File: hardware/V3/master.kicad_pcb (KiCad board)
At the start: 4 copper layers, 40 x 40 mm, 141 parts, among them J1 USB-C, J2 DRILL, J3 DRILL, J4 DRILL, J5 DRILL, J6 STACK-UP-LOW, J7 STACK-DOWN, J8 STACK-UP-LOW, J9 STACK-DOWN, P1 Port A, P2 Port B, P3 Port C, P4 Port D, P5 TSTPT_GND, P6 TSTPT_5V, P7 TSTPT_3V3, P8 Bricklet 5V, P9 Bricklet 3,3V, Q1 2N7002P, SW1 Reset, SW2 Erase, U1 SAM???, U12 LD1117, U13 STMPS2171STR, U2 82400152, U3 TPS22975, U4 AP7333-33SRG, U5 AP7333-33SRG, X1 16Mhz

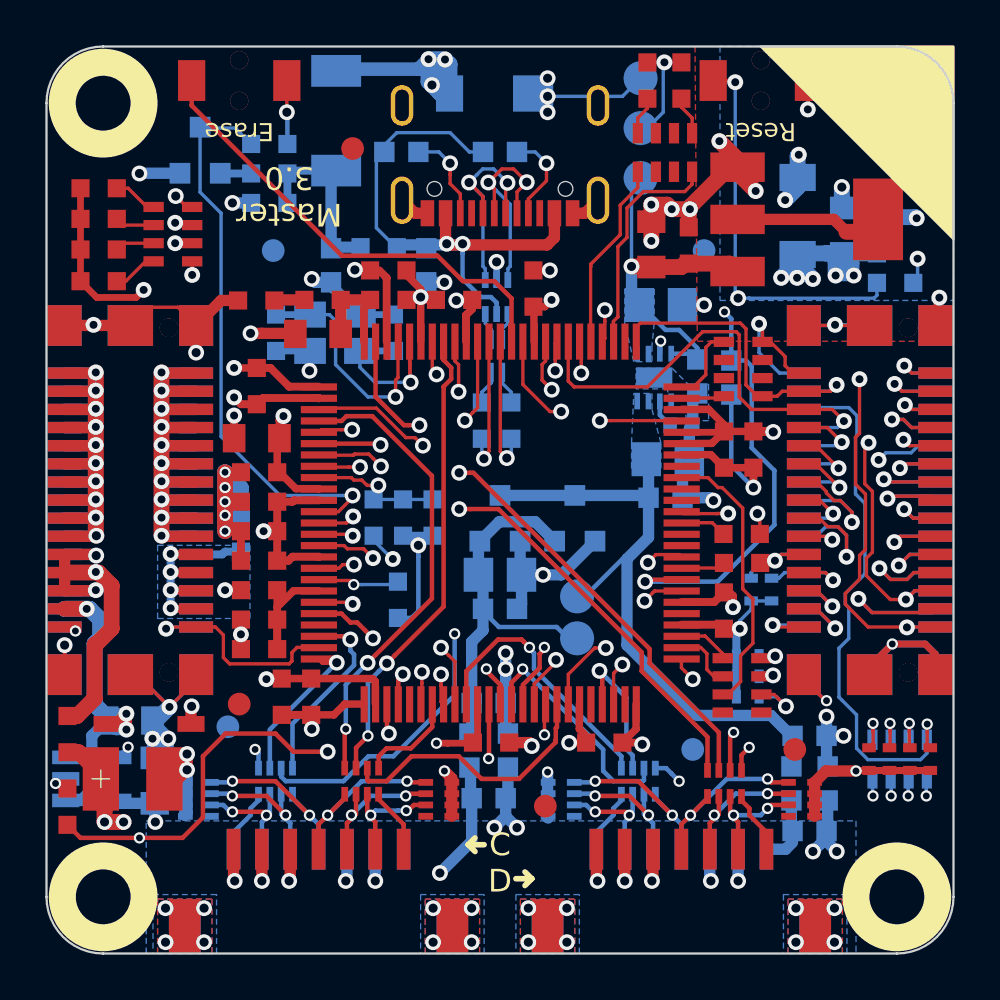
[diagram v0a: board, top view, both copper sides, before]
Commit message: add series resistors for stack connections, change signal connections
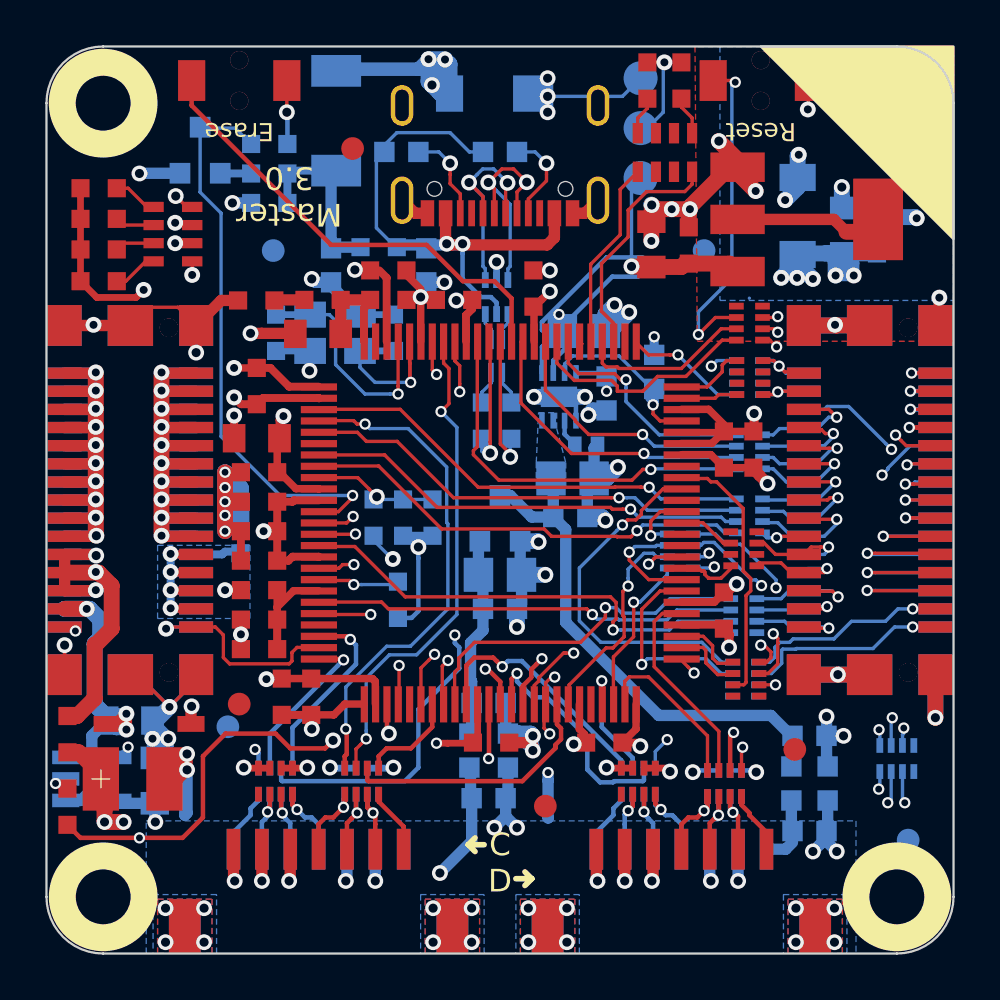
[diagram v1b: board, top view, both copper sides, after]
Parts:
- removed C1, C2, C3, C4, C5, C6, C7, C8, C9: DNP, C0402
- removed P8: Bricklet 5V, kicad-libraries:TSTPT
- removed P9: Bricklet 3,3V, kicad-libraries:TSTPT
- removed R1, R2: 100, R0603
- removed R14: 1k, R0603
- removed RP1, RP2: 100, 0603X4
- removed U5: AP7333-33SRG, kicad-libraries:SOT23-3
- added RP301: 82, kicad-libraries:4X0402, B.Cu at (156.0, 87.9)
- added RP302: 82, kicad-libraries:4X0402, B.Cu at (156.0, 90.7)
- added RP303: 82, kicad-libraries:4X0402, F.Cu at (155.8, 92.2)
- added RP304: 82, kicad-libraries:4X0402, B.Cu at (155.8, 95.1)
- added RP305: 82, kicad-libraries:4X0402, B.Cu at (162.5, 101.4)
- added RP306: 82, kicad-libraries:4X0402, F.Cu at (155.8, 97.9)
- added RP307: 82, kicad-libraries:4X0402, B.Cu at (152.9, 92.2)
- added RP308: 82, kicad-libraries:4X0402, B.Cu at (155.8, 97.9)
- added RP309: 1k, kicad-libraries:4X0402, F.Cu at (156.0, 82.2)
- added RP310: 82, kicad-libraries:4X0402, B.Cu at (156.0, 84.6)
- CP1, CP2: moved to F.Cu
- CP3, CP4: moved to B.Cu
- RP8: footprint 0603X4 -> kicad-libraries:4X0402
- moved Fiducial_Mark 10.3 mm to (163.0, 105.0)
- moved U3 4.29 mm to (147.6, 85.5)
- moved C41 4.29 mm to (148.2, 89.0)
- moved C42 4.29 mm to (148.1, 90.8)
- moved C40 4.29 mm to (148.8, 87.5)
- moved C14 4.07 mm to (149.7, 85.3)
- moved C45 3.59 mm to (148.7, 82.5)
- moved CP1 3.49 mm to (135.1, 102.4), turned to 0 degrees
- moved CP2 3.49 mm to (151.1, 102.4), turned to 0 degrees
- moved CP3 3.49 mm to (138.9, 102.4), turned to 180 degrees
- moved CP4 3.47 mm to (154.9, 102.5), turned to 180 degrees
- moved R7 3.41 mm to (151.8, 84.3), turned to 270 degrees
- moved RP8 0.48 mm to (156.0, 84.6), turned to 90 degrees
- moved FB3 0.08 mm to (133.6, 91.5), turned to 90 degrees
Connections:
- FB3 pad 1: GND -> Net-(FB3-Pad1)
- FB3 pad 2: Net-(FB3-Pad2) -> GND
- J6 pad 1: STACK-SPI-MISO -> Net-(J6-Pad1)
- J6 pad 10: STACK-SELECT-02 -> Net-(J6-Pad10)
- J6 pad 11: STACK-SYNC/JTAG-TCK -> Net-(J6-Pad11)
- J6 pad 12: STACK-SELECT-03 -> Net-(J6-Pad12)
- J6 pad 13: STACK-SER-RXD -> Net-(J6-Pad13)
- J6 pad 14: STACK-SELECT-04 -> Net-(J6-Pad14)
- J6 pad 15: STACK-SER-TXD -> Net-(J6-Pad15)
- J6 pad 16: STACK-SELECT-05 -> Net-(J6-Pad16)
- J6 pad 17: STACK-SER-SCK -> Net-(J6-Pad17)
- J6 pad 18: STACK-SELECT-06 -> Net-(J6-Pad18)
- J6 pad 19: STACK-EX-0-GP00 -> Net-(J6-Pad19)
- J6 pad 2: STACK-I2C-SDA/JTAG-TDI -> Net-(J6-Pad2)
- J6 pad 20: STACK-SELECT-07 -> Net-(J6-Pad20)
- J6 pad 21: STACK-EX-0-GP01 -> Net-(J6-Pad21)
- J6 pad 22: STACK-SELECT-EX-00 -> Net-(J6-Pad22)
- J6 pad 23: STACK-EX-0-GP02 -> Net-(J6-Pad23)
- J6 pad 24: STACK-SELECT-EX-01 -> Net-(J6-Pad24)
- J6 pad 25: STACK-EX-1-GP00 -> Net-(J6-Pad25)
- J6 pad 26: STACK-SER2-RXD -> Net-(J6-Pad26)
- J6 pad 27: STACK-EX-1-GP01 -> Net-(J6-Pad27)
- J6 pad 28: STACK-SER2-TXD -> Net-(J6-Pad28)
- J6 pad 29: STACK-EX-1-GP02 -> Net-(J6-Pad29)
- J6 pad 3: STACK-SPI-MOSI -> Net-(J6-Pad3)
- J6 pad 30: STACK-SER2-RTS -> Net-(J6-Pad30)
- J6 pad 4: STACK-I2C-SCL/JTAG-TDO -> Net-(J6-Pad4)
- J6 pad 5: STACK-SPI-SCLK -> Net-(J6-Pad5)
- J6 pad 6: STACK-SELECT-00 -> Net-(J6-Pad6)
- J6 pad 8: STACK-SELECT-01 -> Net-(J6-Pad8)
- J6 pad 9: STACK-HIGH/JTAG-TMS -> Net-(J6-Pad9)
- J7 pad 1: STACK-SPI-MISO -> Net-(J6-Pad1)
- J7 pad 10: STACK-SELECT-01 -> Net-(J6-Pad8)
- J7 pad 11: STACK-SYNC/JTAG-TCK -> Net-(J6-Pad11)
- J7 pad 12: STACK-SELECT-02 -> Net-(J6-Pad10)
- J7 pad 13: STACK-SER-RXD -> Net-(J6-Pad13)
- J7 pad 14: STACK-SELECT-03 -> Net-(J6-Pad12)
- J7 pad 15: STACK-SER-TXD -> Net-(J6-Pad15)
- J7 pad 16: STACK-SELECT-04 -> Net-(J6-Pad14)
- J7 pad 17: STACK-SER-SCK -> Net-(J6-Pad17)
- J7 pad 18: STACK-SELECT-05 -> Net-(J6-Pad16)
- J7 pad 19: STACK-EX-0-GP00 -> Net-(J6-Pad19)
- J7 pad 2: STACK-I2C-SDA/JTAG-TDI -> Net-(J6-Pad2)
- J7 pad 20: STACK-SELECT-06 -> Net-(J6-Pad18)
- J7 pad 21: STACK-EX-0-GP01 -> Net-(J6-Pad21)
- J7 pad 22: STACK-SELECT-EX-00 -> Net-(J6-Pad22)
- J7 pad 23: STACK-EX-0-GP02 -> Net-(J6-Pad23)
- J7 pad 24: STACK-SELECT-EX-01 -> Net-(J6-Pad24)
- J7 pad 25: STACK-EX-1-GP00 -> Net-(J6-Pad25)
- J7 pad 26: STACK-SER2-RXD -> Net-(J6-Pad26)
- J7 pad 27: STACK-EX-1-GP01 -> Net-(J6-Pad27)
- J7 pad 28: STACK-SER2-TXD -> Net-(J6-Pad28)
- J7 pad 29: STACK-EX-1-GP02 -> Net-(J6-Pad29)
- J7 pad 3: STACK-SPI-MOSI -> Net-(J6-Pad3)
- J7 pad 30: STACK-SER2-RTS -> Net-(J6-Pad30)
- J7 pad 4: STACK-I2C-SCL/JTAG-TDO -> Net-(J6-Pad4)
- J7 pad 5: STACK-SPI-SCLK -> Net-(J6-Pad5)
- J7 pad 8: STACK-SELECT-00 -> Net-(J6-Pad6)
- J8 pad 21: Net-(FB3-Pad2) -> Net-(FB3-Pad1)
- J8 pad 23: Net-(FB3-Pad2) -> Net-(FB3-Pad1)
- J8 pad 25: Net-(FB3-Pad2) -> Net-(FB3-Pad1)
- J8 pad 27: Net-(FB3-Pad2) -> Net-(FB3-Pad1)
- J9 pad 21: Net-(FB3-Pad2) -> Net-(FB3-Pad1)
- J9 pad 23: Net-(FB3-Pad2) -> Net-(FB3-Pad1)
- J9 pad 25: Net-(FB3-Pad2) -> Net-(FB3-Pad1)
- J9 pad 27: Net-(FB3-Pad2) -> Net-(FB3-Pad1)
- P1 pad 4: Net-(CP1-Pad1) -> Net-(CP1-Pad4)
- P1 pad 5: Net-(CP1-Pad2) -> Net-(CP1-Pad3)
- P1 pad 6: Net-(CP1-Pad3) -> Net-(CP1-Pad2)
- P2 pad 4: Net-(CP2-Pad1) -> Net-(CP2-Pad4)
- P2 pad 5: Net-(CP2-Pad2) -> Net-(CP2-Pad3)
- P2 pad 6: Net-(CP2-Pad3) -> Net-(CP2-Pad2)
- P3 pad 4: Net-(CP3-Pad1) -> Net-(CP3-Pad4)
- P3 pad 5: Net-(CP3-Pad2) -> Net-(CP3-Pad3)
- P3 pad 6: Net-(CP3-Pad3) -> Net-(CP3-Pad2)
- P4 pad 4: Net-(CP4-Pad1) -> Net-(CP4-Pad4)
- P4 pad 5: Net-(CP4-Pad2) -> Net-(CP4-Pad3)
- P4 pad 6: Net-(CP4-Pad3) -> Net-(CP4-Pad2)
- RP5 pad 5: Net-(CP1-Pad1) -> Net-(CP1-Pad4)
- RP5 pad 6: Net-(CP1-Pad2) -> Net-(CP1-Pad3)
- RP5 pad 7: Net-(CP1-Pad3) -> Net-(CP1-Pad2)
- RP6 pad 5: Net-(CP2-Pad1) -> Net-(CP2-Pad4)
- RP6 pad 6: Net-(CP2-Pad2) -> Net-(CP2-Pad3)
- RP6 pad 7: Net-(CP2-Pad3) -> Net-(CP2-Pad2)
- RP7 pad 5: Net-(CP3-Pad1) -> Net-(CP3-Pad4)
- RP7 pad 6: Net-(CP3-Pad2) -> Net-(CP3-Pad3)
- RP7 pad 7: Net-(CP3-Pad3) -> Net-(CP3-Pad2)
- RP8 pad 1: STACK-I2C-SCL/JTAG-TDO -> Net-(J6-Pad4)
- RP8 pad 4: STACK-I2C-SDA/JTAG-TDI -> Net-(J6-Pad2)
- RP9 pad 5: Net-(CP4-Pad1) -> Net-(CP4-Pad4)
- RP9 pad 6: Net-(CP4-Pad2) -> Net-(CP4-Pad3)
- RP9 pad 7: Net-(CP4-Pad3) -> Net-(CP4-Pad2)
- U1 pad 31: Net-(RP1-Pad4) -> STACK-SPI-SCLK
- U1 pad 33: Net-(RP1-Pad3) -> STACK-SPI-MOSI
- U1 pad 41: Net-(RP1-Pad2) -> STACK-SPI-MISO
- U1 pad 42: Net-(RP1-Pad1) -> STACK-SPI-SELECT
- U1 pad 49: Net-(U1-Pad49) -> Port-D-CS
- U1 pad 52: Net-(RP2-Pad2) -> STACK-SER-TXD
- U1 pad 53: Net-(RP2-Pad1) -> STACK-SER-RXD
- U1 pad 55: Net-(U1-Pad55) -> Port-D-CLK
- U1 pad 57: STACK-EX-0-GP02 -> STACK-EX-1-GP02
- U1 pad 58: Bricklet_Enable -> STACK-EX-0-GP02
- U1 pad 59: Net-(R1-Pad2) -> STACK-SELECT-EX-01
- U1 pad 6: Port-D-CS -> Net-(U1-Pad6)
- U1 pad 63: Net-(R2-Pad2) -> STACK-SELECT-EX-00
- U1 pad 64: STACK-EX-1-GP01 -> STACK-EX-1-GP00
- U1 pad 66: Net-(U1-Pad66) -> STACK-EX-1-GP01
- U1 pad 67: Net-(RP2-Pad3) -> STACK-SER-SCK
- U1 pad 72: STACK-EX-1-GP00 -> Bricklet_Enable
- U1 pad 81: STACK-EX-1-GP02 -> Net-(U1-Pad81)
- U1 pad 99: Port-D-CLK -> Net-(U1-Pad99)
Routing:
- net Net-(RP1-Pad3): track 27.2 -> 0.00 mm, vias 2 -> 0
- net Net-(RP1-Pad4): track 26.8 -> 0.00 mm, vias 2 -> 0
- net STACK-EX-1-GP00: track 27.9 -> 2.94 mm, vias 3 -> 1
- net Net-(RP1-Pad2): track 22.8 -> 0.00 mm, vias 2 -> 0
- net Net-(RP1-Pad1): track 21.6 -> 0.00 mm, vias 2 -> 0
- net STACK-SPI-SELECT: track 24.1 -> 45.4 mm, vias 1 -> 3
- net STACK-EX-1-GP02: track 30.1 -> 8.90 mm, vias 3 -> 1
- net Net-(J6-Pad1): track 0.00 -> 19.8 mm, vias 0 -> 2
- net Net-(J6-Pad3): track 0.00 -> 19.3 mm, vias 0 -> 2
- net Net-(J6-Pad5): track 0.00 -> 18.7 mm, vias 0 -> 2
- net Port-D-CLK: track 26.3 -> 9.09 mm, vias 2 -> 0
- net Port-D-CS: track 24.5 -> 7.39 mm, vias 2 -> 0
- net STACK-EX-0-GP00: track 23.8 -> 7.09 mm, vias 2 -> 1
- net Net-(J6-Pad13): track 0.00 -> 16.4 mm, vias 0 -> 2
- net Net-(J6-Pad15): track 0.00 -> 15.8 mm, vias 0 -> 2
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- removed copper zone on B.Cu, net Net-(FB3-Pad2)
- removed copper zone on B.Cu, net VSTACK
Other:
- board text removed: "B3V3"
- board text removed: "B5V"

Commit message: routing improved
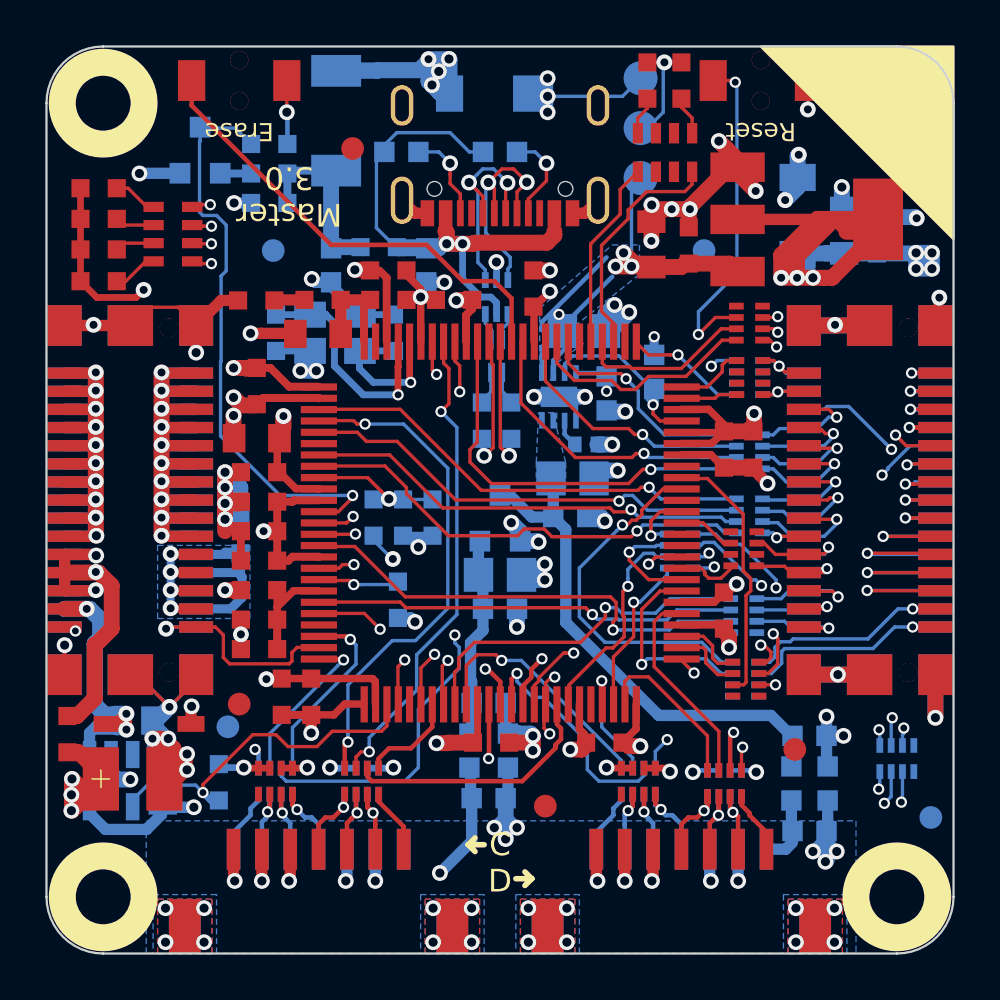
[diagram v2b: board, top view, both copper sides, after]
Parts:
- R17: moved to B.Cu
- moved R17 6.76 mm to (132.6, 102.5)
- moved Fiducial_Mark 1.41 mm to (164.0, 104.0)
- moved U13 0.85 mm to (127.8, 102.4), turned to 180 degrees
- moved C35 0.35 mm to (130.1, 102.4)
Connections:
- net Net-(FB3-Pad1) renamed PGND
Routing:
- net Net-(C27-Pad1): track 74.2 -> 127.2 mm
- net 3V3: track 74.7 -> 98.7 mm, vias 20 -> 22
- net VSTACK: track 106.3 -> 118.8 mm, vias 8 -> 12
- net 3V3-EN: track 25.8 -> 15.6 mm, vias 4 -> 1
- net PGND: track 13.5 -> 22.5 mm
- net Net-(C47-Pad2): track 24.3 -> 33.0 mm
- net GND: track 197.8 -> 203.5 mm, vias 71 -> 74
- net XIN: track 10.3 -> 15.9 mm
- net XOUT: track 8.58 -> 13.7 mm
- net VUSB: track 8.16 -> 13.0 mm
- net GNDD1: track 12.8 -> 15.9 mm, vias 24 -> 26
- net LED2: track 16.2 -> 14.7 mm
- net VCC: track 24.1 -> 22.9 mm
- net Net-(C10-Pad1): track 5.69 -> 6.76 mm
- net STACK-SPI-SELECT: track 45.4 -> 44.4 mm
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- added copper zone on B.Cu, net PGND
- added copper zone on B.Cu, net VSTACK
- removed copper zone on B.Cu, net 3V3
- removed copper zone on F.Cu, net 3V3
- removed copper zone on B.Cu, net GND

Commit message: add ferrites for usb gnd and shield
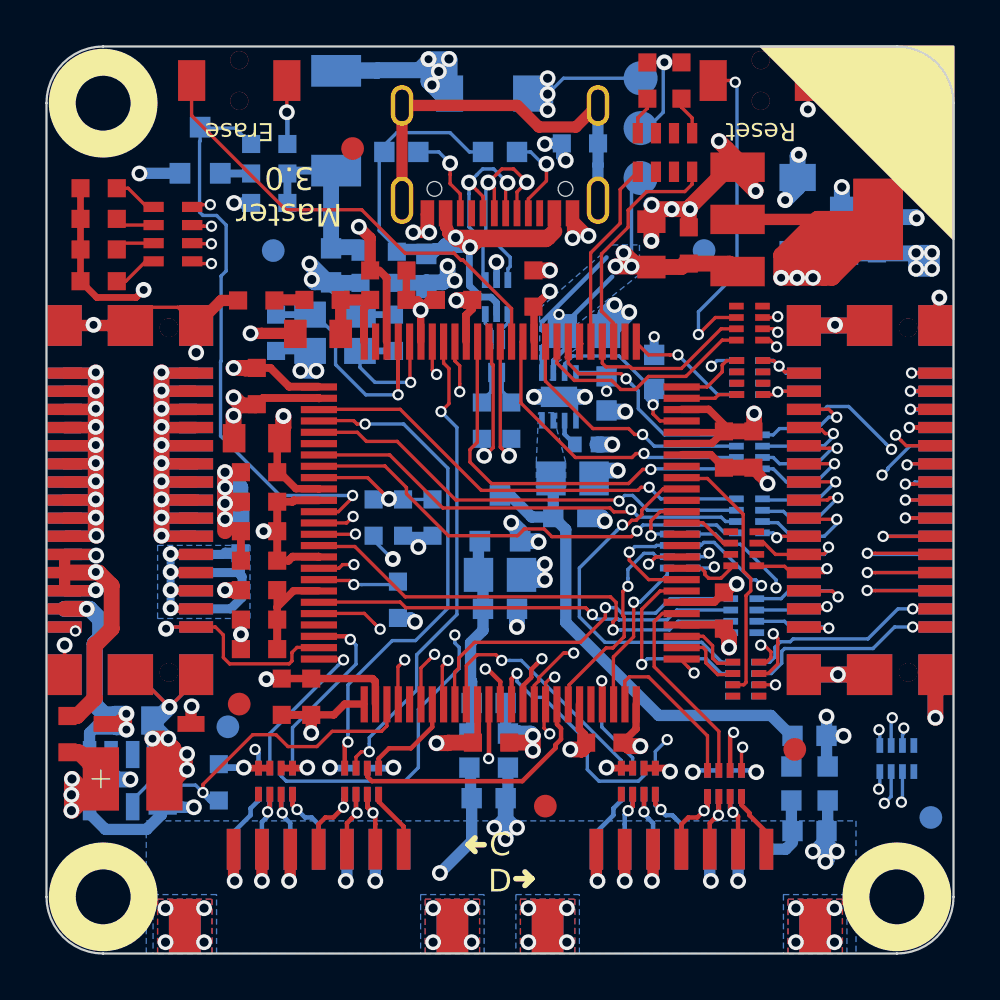
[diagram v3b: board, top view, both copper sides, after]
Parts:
- added FB101: FB, C0603, B.Cu at (139.7, 80.4)
- added FB102: FB, C0603, B.Cu at (148.5, 74.3)
- J1: footprint kicad-libraries:USB-C -> kicad-libraries:USB-C-2
- moved C47 0.25 mm to (141.8, 79.9)
- moved FB1 0.20 mm to (139.7, 79.0)
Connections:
- C47 pad 1: GND -> USB_GND
- J1 pad 6: GND -> USB_GND
- U2 pad 2: GND -> USB_GND
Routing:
- net USB_GND: track 0.00 -> 19.1 mm, vias 0 -> 7
- net Net-(FB102-Pad1): track 0.00 -> 17.8 mm
- net 3V3: track 98.7 -> 107.4 mm
- net XOUT: track 13.7 -> 6.83 mm
- net XIN: track 15.9 -> 12.3 mm
- net Net-(C47-Pad2): track 33.0 -> 31.6 mm
- net GND: track 203.5 -> 204.9 mm, vias 74 -> 75

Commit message: routing improvement
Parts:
- C46, C47: value TBD -> 1uF
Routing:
- net GND: track 204.9 -> 209.1 mm, vias 75 -> 79
- net Net-(C47-Pad2): track 31.6 -> 33.7 mm

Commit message: ordered prototype
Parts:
- added C401: 100nF, C0603, F.Cu at (134.1, 82.6)
- added R301: 82, kicad-libraries:R0402E, B.Cu at (164.2, 101.4)
- FB4: footprint C0603 -> kicad-libraries:R0603F
- moved C36 0.18 mm to (134.1, 81.2)
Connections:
- J7 pad 6: STACK-SPI-SELECT -> Net-(J7-Pad6)
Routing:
- net Net-(C27-Pad1): track 127.2 -> 97.5 mm
- net Net-(J7-Pad6): track 0.00 -> 22.9 mm, vias 0 -> 2
- net STACK-SPI-SELECT: track 44.4 -> 21.8 mm, vias 3 -> 2
- net GND: track 209.1 -> 215.6 mm, vias 79 -> 82
- net Port-A-CLK: track 17.4 -> 14.5 mm, vias 2 -> 1
- net STACK-RESET: track 27.5 -> 29.5 mm
- net LED3: track 19.0 -> 18.4 mm
